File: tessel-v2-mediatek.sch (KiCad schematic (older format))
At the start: 49 parts, among them U201 MT7620N, X201 20MHz

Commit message: 0603 resistor swapped
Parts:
- C202, C230, C232: footprint SMD_Packages:SMD-0603 -> tm-kicad-lib:SMD-0603-C
- C203, C204, C205, C206, C207, C209, C210, C212, C213, C214, C215, C216, C218, C219, C220, C221, C222, C224, C225, C226, C227, C228, C229, C231, C233, C234, C235, C236, C241, C242, C243, C244: footprint tm-kicad-lib:SMD-0402 -> tm-kicad-lib:SMD-0402-C
- L201, L202, R201, R202, R203, R204: footprint tm-kicad-lib:SMD-0402 -> tm-kicad-lib:SMD-0402-R

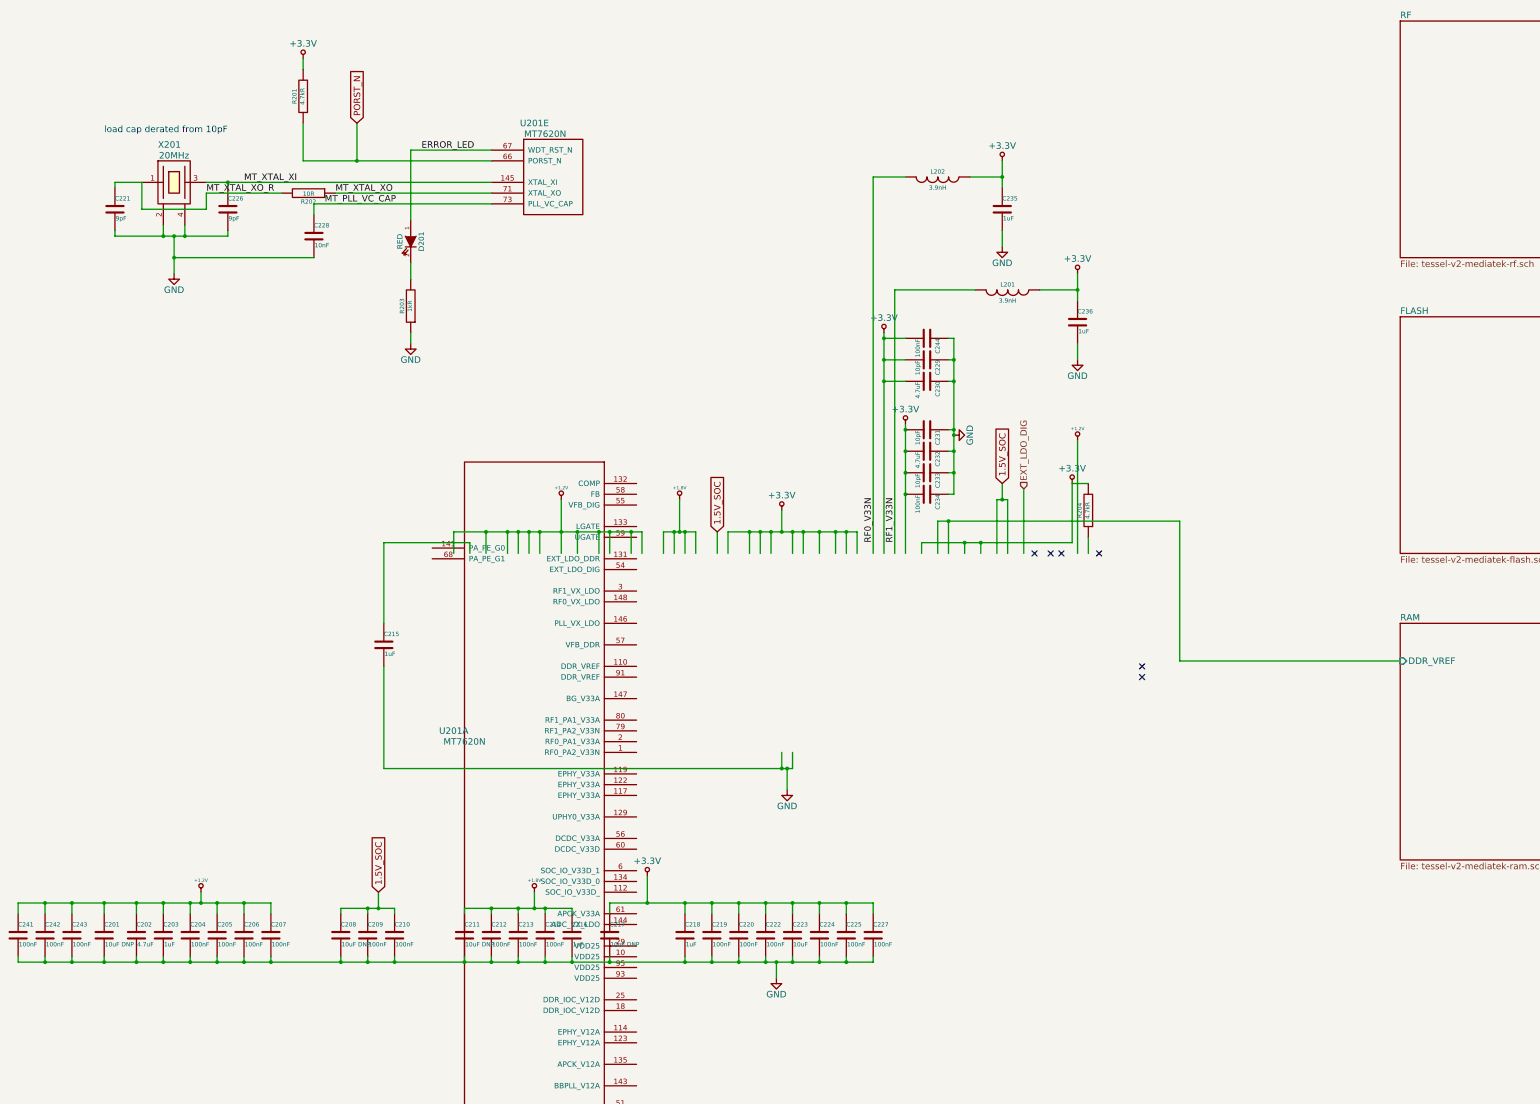
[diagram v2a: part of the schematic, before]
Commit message: working towards pin muxing for v2v3 and general schematic cleanup
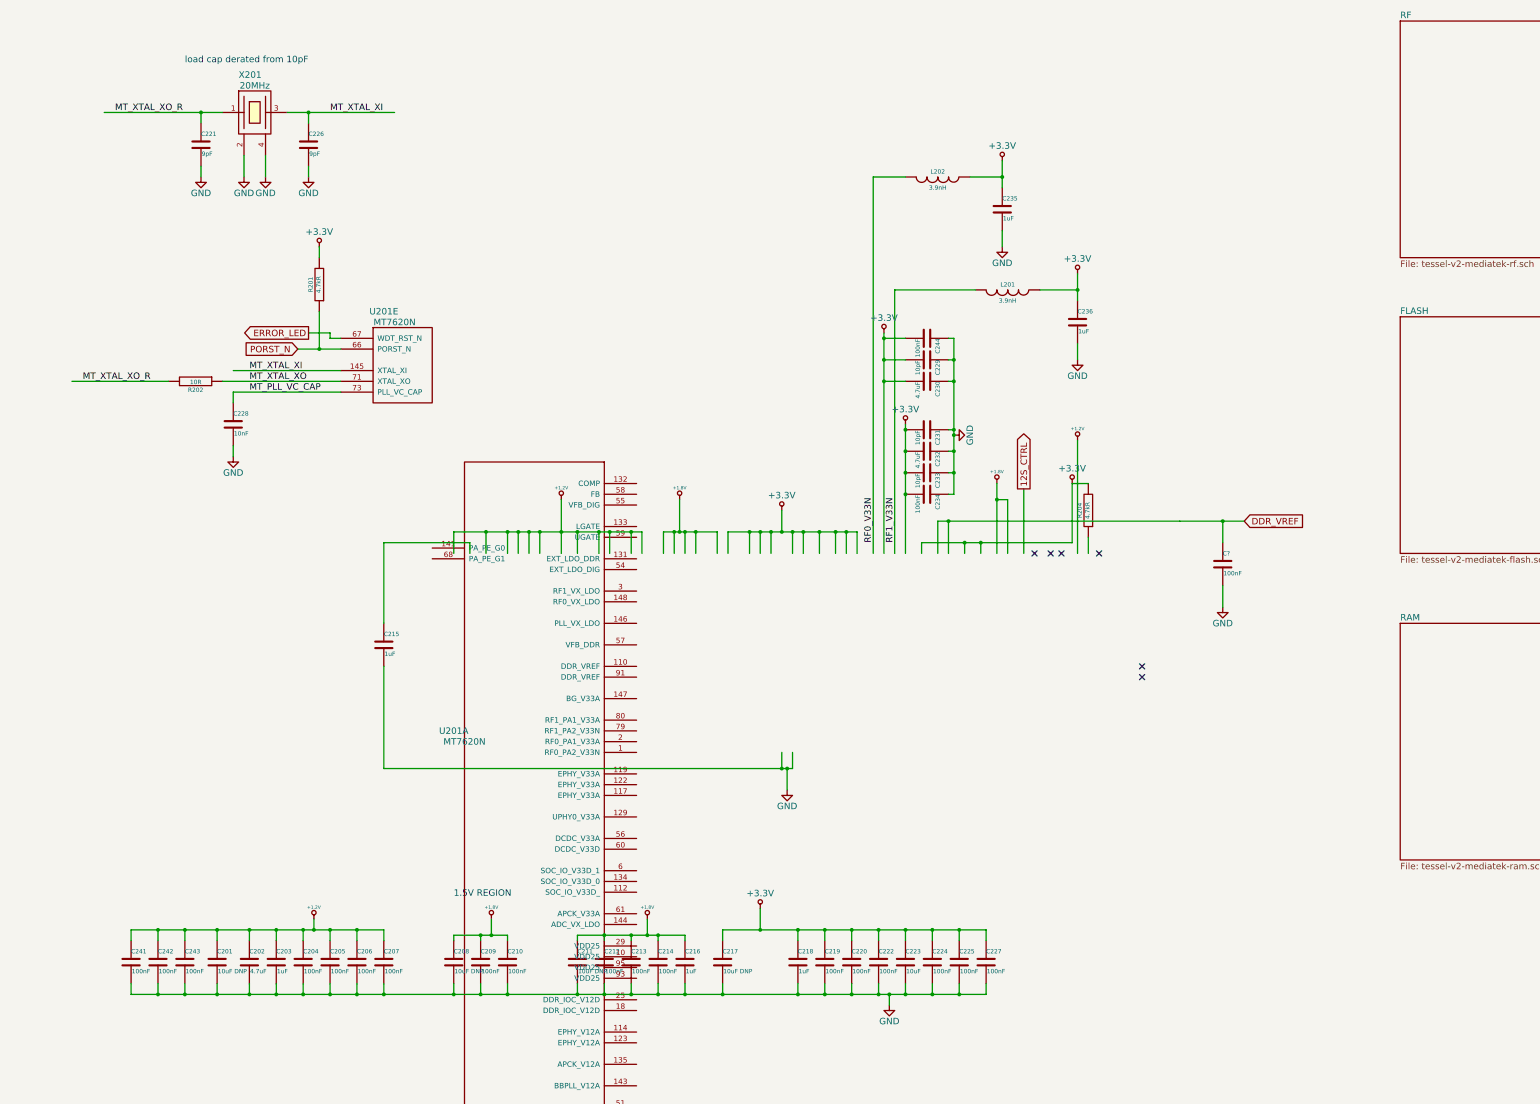
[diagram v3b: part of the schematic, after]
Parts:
- removed D201: RED, LEDs:LED-0603, symbol LED
- removed R203: 1kR, tm-kicad-lib:SMD-0402-R, symbol R
- added C?: 100nF, tm-kicad-lib:SMD-0402-C, symbol C
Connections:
- net labels added: 12S_CTRL, DDR_VREF
- net labels removed: 1.5V_SOC, EXT_LDO_DIG
- wire segments 175 -> 267
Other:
- note added: "1.5V REGION"
- moved on the sheet: C201, C202, C203, C204, C205, C206, C207, C208, C209, C210, C211, C212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

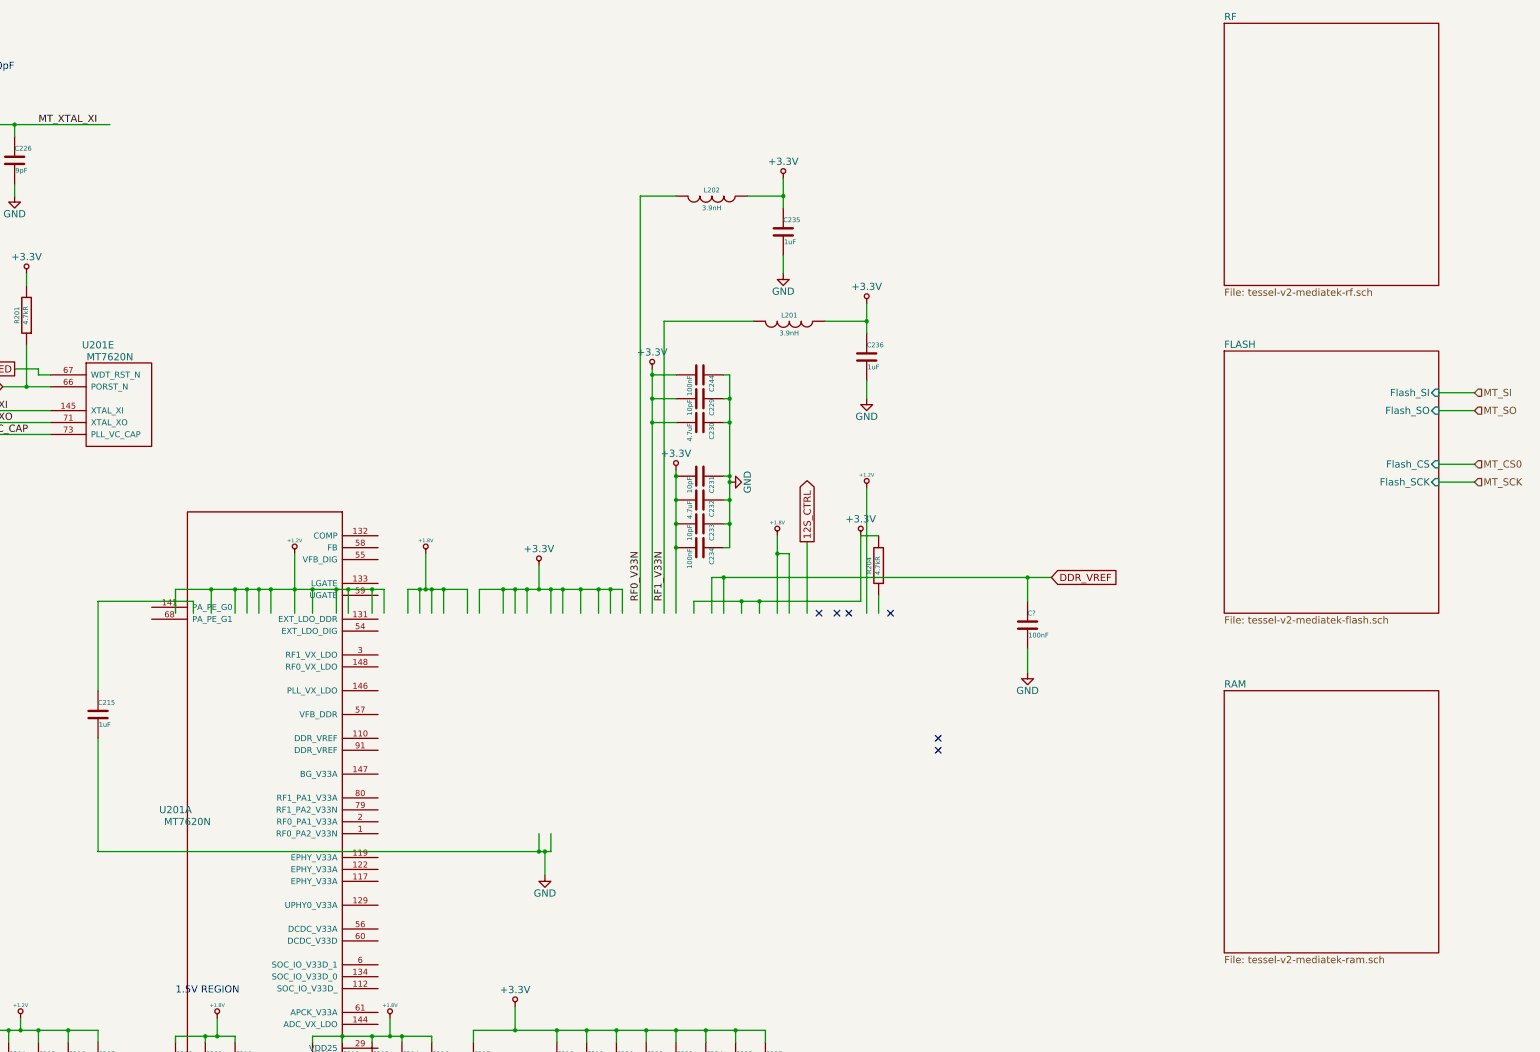
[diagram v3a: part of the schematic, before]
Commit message: most schematic changes done, major refactoring underway
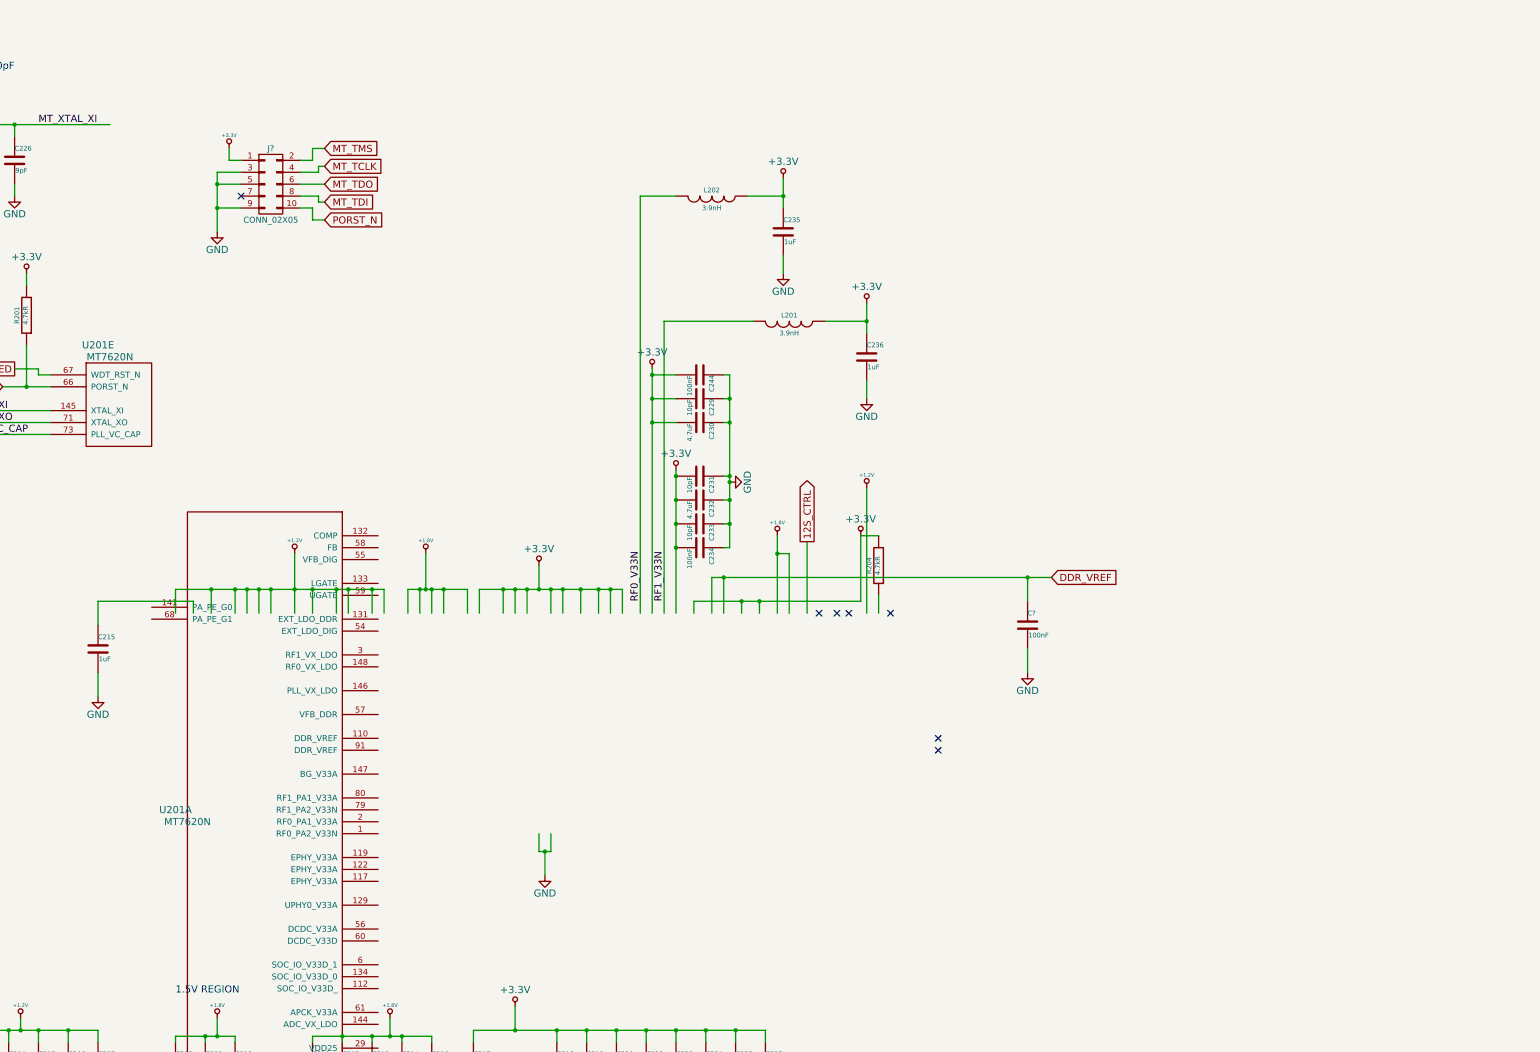
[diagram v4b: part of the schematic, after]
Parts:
- added J?: CONN_02X05, tm-kicad-lib:CONN_02x05_0.05in, symbol CONN_02X05
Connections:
- net labels added: MT_TCLK, MT_TDI, MT_TDO, MT_TMS
- net labels removed: MT_CS0, MT_SCK, MT_SI, MT_SO
- wire segments 267 -> 282
- no-connect marks 6 -> 7
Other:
- moved on the sheet: C215
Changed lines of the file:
@@
 $Descr B 17000 11000
 encoding utf-8
-Sheet 2 8
+Sheet 2 9
 Title "Tessel v2"
 Date ""
@@
 Comment4 ""
 $EndDescr
-$Sheet
-S 13450 6550 1800 2200
-U 548CC02E
-F0 "RAM" 60
-F1 "tessel-v2-mediatek-ram.sch" 60
-$EndSheet
-$Sheet
-S 13450 3700 1800 2200
-U 548CC15A
-F0 "FLASH" 60
-F1 "tessel-v2-mediatek-flash.sch" 60
-F2 "Flash_SI" I R 15250 4050 60
-F3 "Flash_SO" I R 15250 4200 60
-F4 "Flash_CS" I R 15250 4650 60
-F5 "Flash_SCK" I R 15250 4800 60
-$EndSheet
-$Sheet
-S 13450 950  1800 2200
-U 548CC15D
-F0 "RF" 60
-F1 "tessel-v2-mediatek-rf.sch" 60
-$EndSheet
 $Comp
 L GND #PWR01
@@
 L C C215
 U 1 1 548FE2F7
-P 4000 6750
-F 0 "C215" H 4000 6850 40  0000 L CNN
-F 1 "1uF" H 4006 6665 40  0000 L CNN
-F 2 "tm-kicad-lib:SMD-0402-C" H 4038 6600 30  0001 C CNN
-F 3 "" H 4000 6750 60  0000 C CNN
-	1    4000 6750
+P 4000 6200
+F 0 "C215" H 4000 6300 40  0000 L CNN
+F 1 "1uF" H 4006 6115 40  0000 L CNN
+F 2 "tm-kicad-lib:SMD-0402-C" H 4038 6050 30  0001 C CNN
+F 3 "" H 4000 6200 60  0000 C CNN
+	1    4000 6200
 	1    0    0    -1
 $EndComp
@@
 	1    0    0    -1
 $EndComp
-Text HLabel 15550 4050 2    60   Input ~ 0
-MT_SI
-Text HLabel 15550 4200 2    60   Input ~ 0
-MT_SO
-Text HLabel 15550 4650 2    60   Input ~ 0
-MT_CS0
-Text HLabel 15550 4800 2    60   Input ~ 0
-MT_SCK
 $Comp
 L R R201
@@
 	7700 7750 7700 7900
 Wire Wire Line
-	4000 7900 7700 7900
-Wire Wire Line
 	7700 7900 7750 7900
 Wire Wire Line
@@
 	4800 5800 4000 5800
 Wire Wire Line
-	4000 5800 4000 6550
-Wire Wire Line
-	4000 6950 4000 7900
-Connection ~ 7700 7900
+	4000 5800 4000 6000
 Wire Wire Line
 	4950 5900 4950 5700
@@
 	9000 5900 9000 5800
 Wire Wire Line
-	11400 5600 9250 5600
-Wire Wire Line
-	9250 5600 9150 5600
+	9150 5600 9250 5600
+Wire Wire Line
+	9250 5600 11800 5600
+Wire Wire Line
+	11800 5600 12000 5600
 Wire Wire Line
 	9150 5600 9150 5900
@@
 Connection ~ 5150 10000
 Connection ~ 4900 10000
-Wire Wire Line
-	15250 4050 15550 4050
-Wire Wire Line
-	15250 4200 15550 4200
-Wire Wire Line
-	15250 4650 15550 4650
-Wire Wire Line
-	15250 4800 15550 4800
 Wire Wire Line
 	3400 3650 3400 4000
@@
 DDR_VREF
 Wire Wire Line
-	11800 5800 11800 5600
+	11800 5600 11800 5800
 Connection ~ 11800 5600
 $Comp
@@
 Wire Wire Line
 	11800 6200 11800 6400
-Wire Wire Line
-	11400 5600 11800 5600
-Wire Wire Line
-	11800 5600 12000 5600
+$Comp
+L GND #PWR?
+U 1 1 54EC7EE4
+P 4000 6600
+F 0 "#PWR?" H 4000 6350 60  0001 C CNN
+F 1 "GND" H 4000 6450 60  0000 C CNN
+F 2 "" H 4000 6600 60  0000 C CNN
+F 3 "" H 4000 6600 60  0000 C CNN
+	1    4000 6600
+	1    0    0    -1
+$EndComp
+Wire Wire Line
+	4000 6600 4000 6400
+Text GLabel 5900 2600 2    60   Input ~ 0
+PORST_N
+$Comp
+L CONN_02X05 J?
+U 1 1 54EDE1A1
+P 5450 2300
+F 0 "J?" H 5450 2600 50  0000 C CNN
+F 1 "CONN_02X05" H 5450 2000 50  0000 C CNN
+F 2 "tm-kicad-lib:CONN_02x05_0.05in" H 5450 1100 60  0001 C CNN
+F 3 "" H 5450 1100 60  0000 C CNN
+	1    5450 2300
+	1    0    0    -1
+$EndComp
+$Comp
+L GND #PWR?
+U 1 1 54EDE1A8
+P 5000 2700
+F 0 "#PWR?" H 5000 2450 60  0001 C CNN
+F 1 "GND" H 5000 2550 60  0000 C CNN
+F 2 "" H 5000 2700 60  0000 C CNN
+F 3 "" H 5000 2700 60  0000 C CNN
+	1    5000 2700
+	1    0    0    -1
+$EndComp
+$Comp
+L +3.3V #PWR?
+U 1 1 54EDE1AE
+P 5100 2000
+F 0 "#PWR?" H 5100 1960 30  0001 C CNN
+F 1 "+3.3V" H 5100 2110 30  0000 C CNN
+F 2 "" H 5100 2000 60  0000 C CNN
+F 3 "" H 5100 2000 60  0000 C CNN
+	1    5100 2000
+	1    0    0    -1
+$EndComp
+NoConn ~ 5200 2400
+Text GLabel 5900 2000 2    60   Input ~ 0
+MT_TMS
+Text GLabel 5900 2150 2    60   Input ~ 0
+MT_TCLK
+Text GLabel 5900 2450 2    60   Input ~ 0
+MT_TDI
+Text GLabel 5900 2300 2    60   Input ~ 0
+MT_TDO
+Wire Wire Line
+	5800 2600 5900 2600
+Wire Wire Line
+	5800 2500 5800 2600
+Wire Wire Line
+	5850 2450 5850 2400
+Wire Wire Line
+	5900 2450 5850 2450
+Wire Wire Line
+	5800 2000 5900 2000
+Wire Wire Line
+	5800 2100 5800 2000
+Wire Wire Line
+	5850 2150 5850 2200
+Wire Wire Line
+	5900 2150 5850 2150
+Wire Wire Line
+	5100 2000 5100 2100
+Wire Wire Line
+	5100 2100 5200 2100
+Wire Wire Line
+	5700 2100 5800 2100
+Wire Wire Line
+	5850 2200 5700 2200
+Wire Wire Line
+	5700 2300 5900 2300
+Wire Wire Line
+	5850 2400 5700 2400
+Wire Wire Line
+	5700 2500 5800 2500
+Wire Wire Line
+	5200 2200 5000 2200
+Wire Wire Line
+	5000 2200 5000 2300
+Wire Wire Line
+	5000 2300 5000 2500
+Wire Wire Line
+	5000 2500 5000 2700
+Wire Wire Line
+	5200 2300 5000 2300
+Connection ~ 5000 2300
+Wire Wire Line
+	5000 2500 5200 2500
+Connection ~ 5000 2500
 $EndSCHEMATC
